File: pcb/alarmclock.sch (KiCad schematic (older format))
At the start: 2 parts

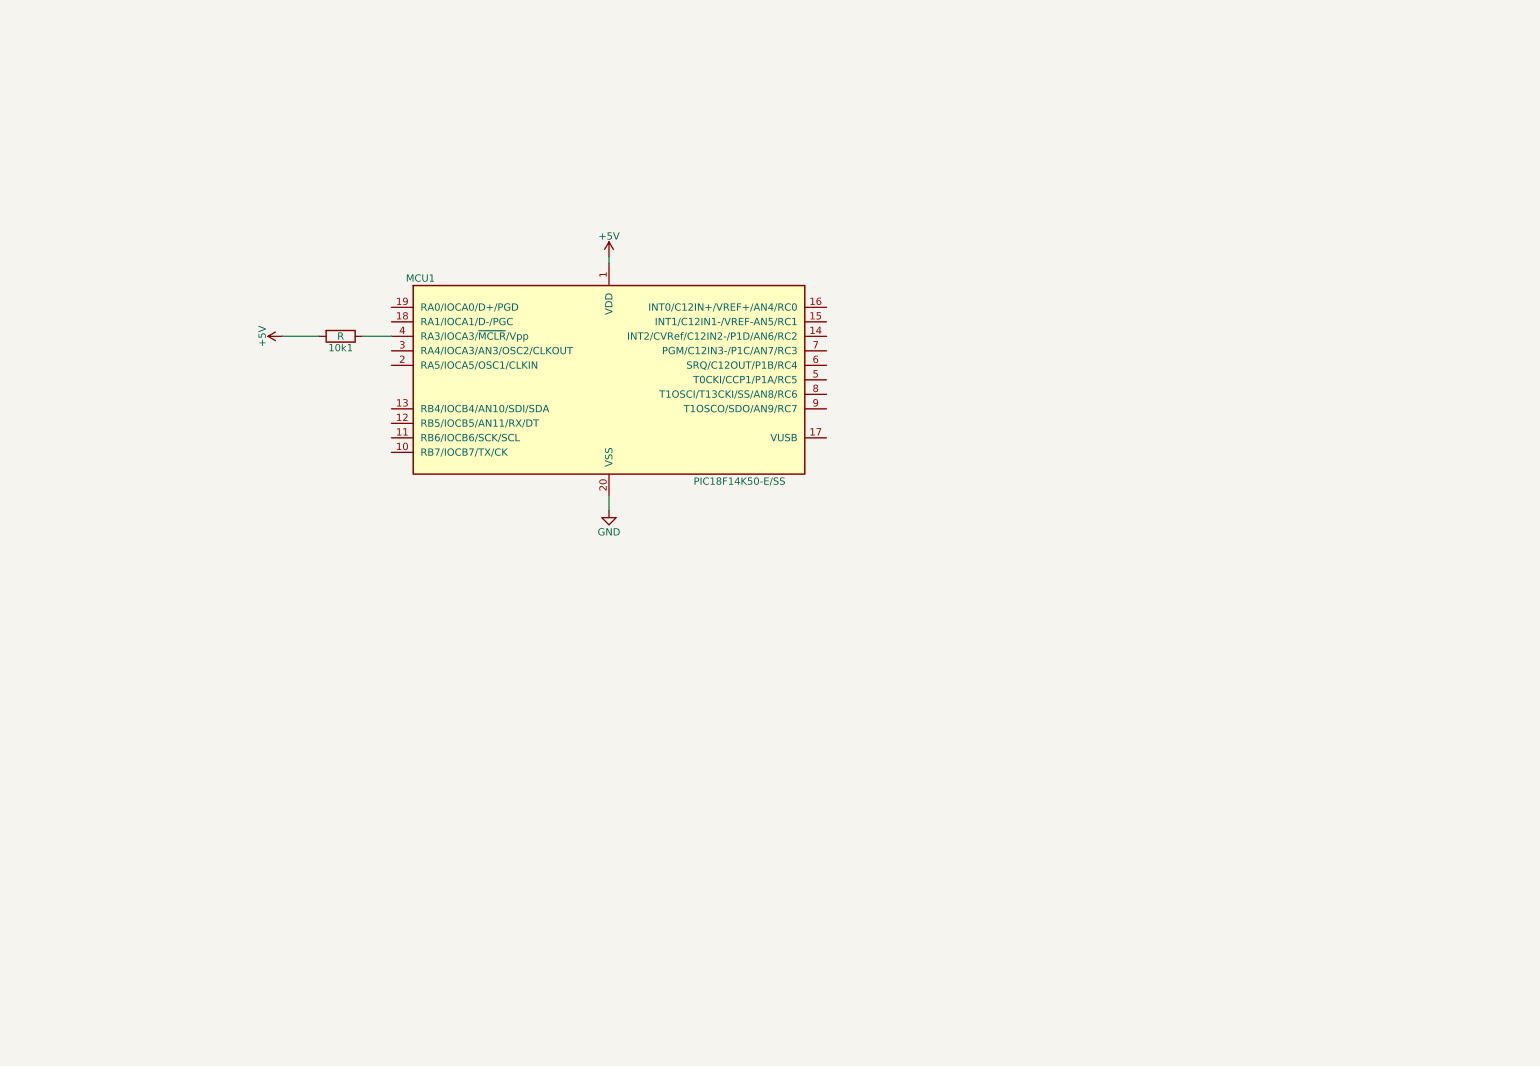
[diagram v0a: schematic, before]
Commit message: Schematic done
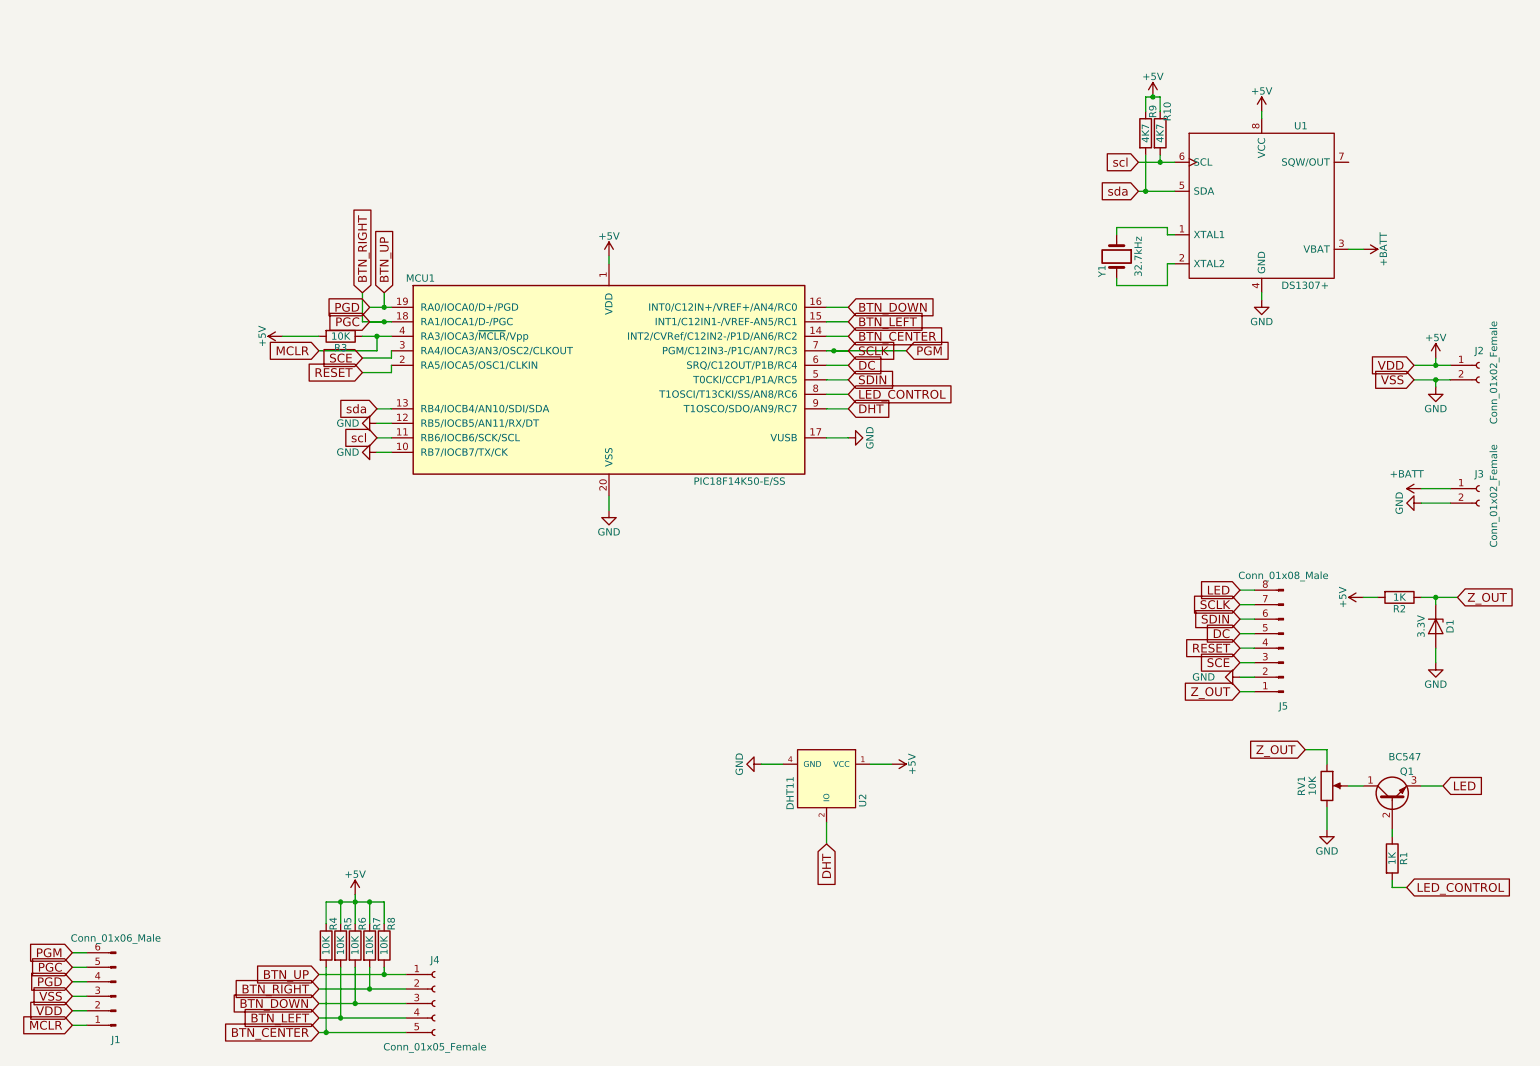
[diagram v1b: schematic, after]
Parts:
- added D1: 3.3V, Diodes_THT:D_A-405_P12.70mm_Horizontal, symbol D_Zener
- added J1: Conn_01x06_Male, Pin_Headers:Pin_Header_Straight_1x06_Pitch1.00mm, symbol Conn_01x06_Male
- added J2, J3: Conn_01x02_Female, Pin_Headers:Pin_Header_Straight_1x02_Pitch2.54mm, symbol Conn_01x02_Female
- added J4: Conn_01x05_Female, Pin_Headers:Pin_Header_Straight_1x05_Pitch2.00mm, symbol Conn_01x05_Female
- added J5: Conn_01x08_Male, Pin_Headers:Pin_Header_Straight_1x08_Pitch2.54mm, symbol Conn_01x08_Male
- added Q1: BC547, TO_SOT_Packages_THT:TO-92_Molded_Narrow, symbol BC547
- added R1, R2: 1K, Resistors_THT:R_Axial_DIN0516_L15.5mm_D5.0mm_P25.40mm_Horizontal, symbol R
- added R10, R9: 4K7, Resistors_THT:R_Axial_DIN0516_L15.5mm_D5.0mm_P25.40mm_Horizontal, symbol R
- added R4, R5, R6, R7, R8: 10K, Resistors_THT:R_Axial_DIN0516_L15.5mm_D5.0mm_P25.40mm_Horizontal, symbol R
- added RV1: 10K, Potentiometers:Potentiometer_Alps_RK097_Single_Vertical, symbol POT
- added U1: DS1307+, Housings_DIP:DIP-8_W7.62mm_Socket_LongPads, symbol DS1307+
- added U2: DHT11, Pin_Headers:Pin_Header_Straight_1x04_Pitch2.00mm, symbol DHT11
- added Y1: 32.7kHz, Crystals:Crystal_Round_d2.0mm_Vertical, symbol Crystal
- R3: renamed from 10k1; value R -> 10K; footprint Resistors_THT:R_Axial_DIN0922_L20.0mm_D9.0mm_P25.40mm_Horizontal -> Resistors_THT:R_Axial_DIN0516_L15.5mm_D5.0mm_P25.40mm_Horizontal
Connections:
- net +5V: now also J1.2 (Pin_2), J2.1 (Pin_1), R10.1, R2.2, R4.1, R5.1, R6.1, R7.1, R8.1, R9.1, U1.8 (VCC), U2.1 (VCC)
- net GND: now also MCU1.10 (RB7/IOCB7/TX/CK), MCU1.12 (RB5/IOCB5/AN11/RX/DT), MCU1.17 (VUSB), D1.2 (A), J1.3 (Pin_3), J2.2 (Pin_2), J3.2 (Pin_2), J5.2 (Pin_2), RV1.3, U1.4 (GND), U2.4 (GND)
- net scl: now reaches MCU1.11 (RB6/IOCB6/SCK/SCL)
- net scl: now also R10.2, U1.6 (SCL)
- net sda: now reaches MCU1.13 (RB4/IOCB4/AN10/SDI/SDA)
- net sda: now also R9.2, U1.5 (SDA)
- net BTN_CENTER: now reaches MCU1.14 (INT2/CVRef/C12IN2-/P1D/AN6/RC2)
- net BTN_CENTER: now also J4.5 (Pin_5), R4.2
- net BTN_LEFT: now reaches MCU1.15 (INT1/C12IN1-/VREF-AN5/RC1)
- net BTN_LEFT: now also J4.4 (Pin_4), R5.2
- net BTN_DOWN: now reaches MCU1.16 (INT0/C12IN+/VREF+/AN4/RC0)
- net BTN_DOWN: now also J4.3 (Pin_3), R6.2
- net BTN_RIGHT: now reaches MCU1.18 (RA1/IOCA1/D-/PGC)
- net BTN_RIGHT: now also J1.5 (Pin_5), J4.2 (Pin_2), R7.2
- net BTN_UP: now reaches MCU1.19 (RA0/IOCA0/D+/PGD)
- net BTN_UP: now also J1.4 (Pin_4), J4.1 (Pin_1), R8.2
- net RESET: now reaches MCU1.2 (RA5/IOCA5/OSC1/CLKIN)
- net RESET: now also J5.4 (Pin_4)
- net SCE: now reaches MCU1.3 (RA4/IOCA3/AN3/OSC2/CLKOUT)
- net SCE: now also J5.3 (Pin_3)
- net MCLR: now reaches MCU1.4 (RA3/IOCA3/~MCLR~/Vpp), R3.1
- net MCLR: now also J1.1 (Pin_1)
- net SDIN: now reaches MCU1.5 (T0CKI/CCP1/P1A/RC5)
- net SDIN: now also J5.6 (Pin_6)
- net DC: now reaches MCU1.6 (SRQ/C12OUT/P1B/RC4)
- net DC: now also J5.5 (Pin_5)
- net PGM: now reaches MCU1.7 (PGM/C12IN3-/P1C/AN7/RC3)
- net PGM: now also J1.6 (Pin_6), J5.7 (Pin_7)
- net LED_CONTROL: now reaches MCU1.8 (T1OSCI/T13CKI/SS/AN8/RC6)
- net LED_CONTROL: now also R1.2
- net DHT: now reaches MCU1.9 (T1OSCO/SDO/AN9/RC7)
- net DHT: now also U2.2 (IO)
- new net: U1.1 (XTAL1), Y1.1
- new net: U1.2 (XTAL2), Y1.2
- new net: Q1.1 (C), RV1.2
- new net: Q1.2 (B), R1.1
- new net +BATT: J3.1 (Pin_1), U1.3 (VBAT)
- new net LED: J5.8 (Pin_8), Q1.3 (E)
- new net Z_OUT: D1.1 (K), J5.1 (Pin_1), R2.1, RV1.1

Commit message: Some adjustments in schematic
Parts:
- added BZ1: Buzzer, Buzzers_Beepers:Buzzer_12x9.5RM7.6, symbol Buzzer
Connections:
- net GND: now also BZ1.2 (+); no longer MCU1.10 (RB7/IOCB7/TX/CK)
- new net BUZZER: BZ1.1 (-), MCU1.10 (RB7/IOCB7/TX/CK)
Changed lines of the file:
@@
 L GND #PWR019
 U 1 1 5A9478AC
-P 3250 3450
-F 0 "#PWR019" H 3250 3200 50  0001 C CNN
-F 1 "GND" V 3250 3250 50  0000 C CNN
-F 2 "" H 3250 3450 50  0001 C CNN
-F 3 "" H 3250 3450 50  0001 C CNN
-	1    3250 3450
+P 4900 6400
+F 0 "#PWR019" H 4900 6150 50  0001 C CNN
+F 1 "GND" V 4900 6200 50  0000 C CNN
+F 2 "" H 4900 6400 50  0001 C CNN
+F 3 "" H 4900 6400 50  0001 C CNN
+	1    4900 6400
 	0    1    1    0
 $EndComp
 Wire Wire Line
 	3250 3250 3350 3250
-Wire Wire Line
-	3350 3450 3250 3450
 Wire Wire Line
 	6500 3350 6350 3350
@@
 	8650 1000 8650 1100
 Connection ~ 8600 1000
+$Comp
+L Buzzer BZ1
+U 1 1 5A9459FB
+P 5050 6300
+F 0 "BZ1" H 5200 6350 50  0000 L CNN
+F 1 "Buzzer" H 5200 6250 50  0000 L CNN
+F 2 "Buzzers_Beepers:Buzzer_12x9.5RM7.6" V 5025 6400 50  0001 C CNN
+F 3 "" V 5025 6400 50  0001 C CNN
+	1    5050 6300
+	1    0    0    -1
+$EndComp
+Text GLabel 4900 6200 0    60   Input ~ 0
+BUZZER
+Wire Wire Line
+	4950 6200 4900 6200
+Wire Wire Line
+	4900 6400 4950 6400
+Text GLabel 3250 3450 0    60   Input ~ 0
+BUZZER
+Wire Wire Line
+	3250 3450 3350 3450
 $EndSCHEMATC

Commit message: updates
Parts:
- removed J2: Conn_01x02_Female, Pin_Headers:Pin_Header_Straight_1x02_Pitch2.54mm, symbol Conn_01x02_Female
- removed RV1: 10K, Potentiometers:Potentiometer_Alps_RK097_Single_Vertical, symbol POT
- added BT1: CR2032, Battery_Holders:Keystone_1058_1x2032-CoinCell, symbol Battery_Cell
- added BT2: 6V, Pin_Headers:Pin_Header_Straight_1x02_Pitch1.27mm, symbol Battery_Cell
- added D2: D, Diodes_THT:D_5W_P10.16mm_Horizontal, symbol D
- added Q2, Q3: BC547, TO_SOT_Packages_THT:TO-92_Molded_Narrow, symbol BC547
- added R11: 10K, Resistors_THT:R_Axial_DIN0516_L15.5mm_D5.0mm_P25.40mm_Horizontal, symbol R
- added SW1: SW_Push, Buttons_Switches_THT:SW_PUSH_6mm, symbol SW_Push
- added U3: MCP23017, SMD_Packages:SOIC-28, symbol MCP23017
- D1: value 3.3V -> 2.7V
- R2: value 1K -> 120
- R3: value 10K -> 1K
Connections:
- net Z_OUT is gone; now on net 3.3V: D1.1 (K), J5.1 (Pin_1), R2.1
- net +BATT: no longer U1.3 (VBAT)
- net BUZZER: now also R3.2; no longer BZ1.1 (-)
- net GND: now also Q1.3 (E), BT1.2 (-), BT2.2 (-), Q2.3 (E), Q3.3 (E), SW1.1, U3.10 (GND); no longer BZ1.2 (+), D1.2 (A), J1.3 (Pin_3)
- net LED: no longer Q1.3 (E)
- net MCLR: now also R11.1, SW1.2; no longer R3.1
- net 3.3V: now reaches Q1.1 (C)
- net 3.3V: now also Q2.1 (C)
- net +5V renamed 5.5V
- net 5.5V: now also D2.1 (K), R11.2, U3.9 (VCC); no longer J1.2 (Pin_2), R2.2, R3.2
- new net: BT1.1 (+), U1.3 (VBAT)
- new net: D1.2 (A), Q2.2 (B)
- new net: BZ1.2 (+), Q3.1 (C)
- new net: Q3.2 (B), R3.1
- new net 6V: BT2.1 (+), BZ1.1 (-), D2.2 (A), R2.2
- new net VDD: J1.2 (Pin_2)
- new net VSS: J1.3 (Pin_3)
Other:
- moved on the sheet: BZ1, D1, R2
